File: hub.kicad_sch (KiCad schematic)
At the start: 13 parts, among them J1 USB_C_Receptacle_USB2.0_16P, U1 ADuM4165, U2 USBLC6-2SC6, Y1 24MHz

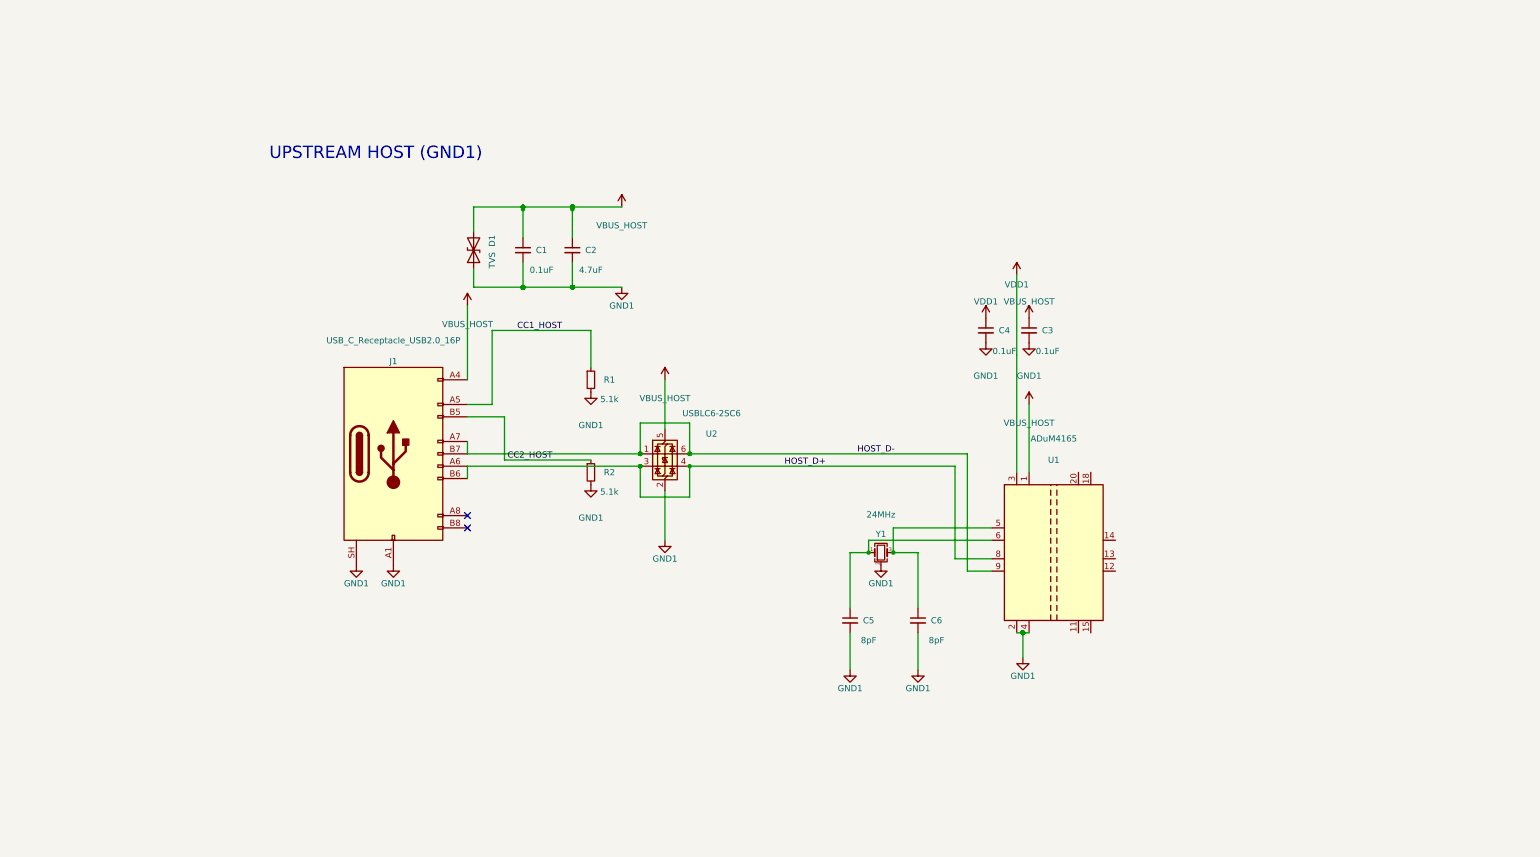
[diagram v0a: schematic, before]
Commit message: feat(revb/sch): upstream CC current-advertisement sensing
Task 4: adds the CC1/CC2 comparator sensing circuit (U3 TLV7042DDFR, R3-R9,
C7-C8, Q1-Q2, D2) that produces HOST_PWR_OK from a VBUS_HOST-referenced
0.66V divider, per decision record section 4.2. Wire-OR polarity is
inverting-comparator + pull-up + NMOS inverter, not the brief's original
either/or. Adds design-note text recording the threshold rationale, the
VBUS_HOST-only constraint, the VCONN false-high caveat, and the R_EN
sizing math.
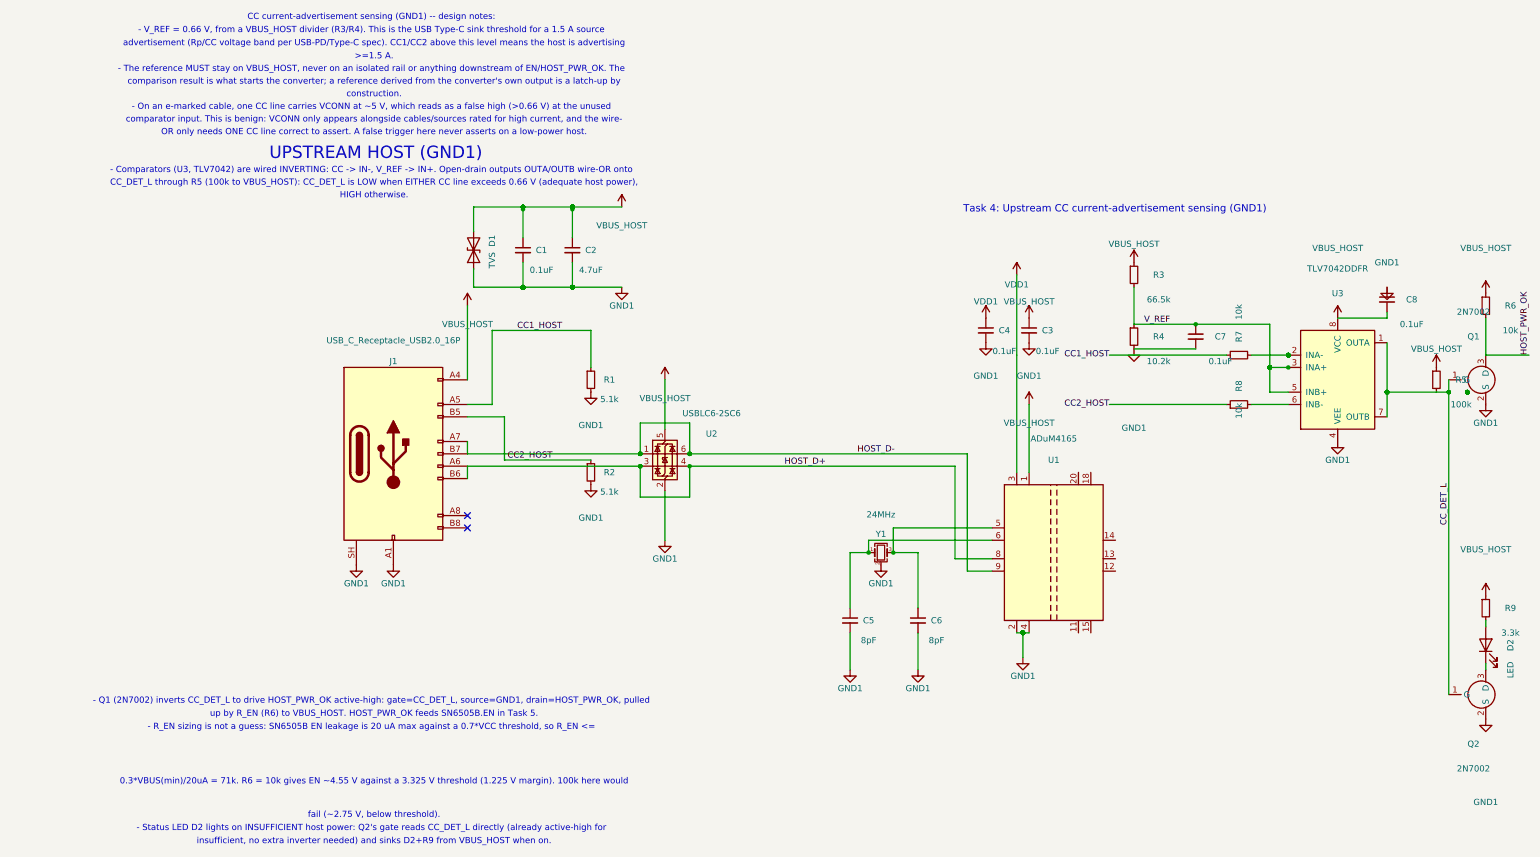
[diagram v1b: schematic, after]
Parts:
- added C7, C8: 0.1uF, symbol Device:C_Small
- added D2: LED, symbol Device:LED
- added Q1, Q2: 2N7002, symbol isolator-lib:2N7002
- added R3: 66.5k, symbol Device:R_Small
- added R4: 10.2k, symbol Device:R_Small
- added R5: 100k, symbol Device:R_Small
- added R6, R7, R8: 10k, symbol Device:R_Small
- added R9: 3.3k, symbol Device:R_Small
- added U3: TLV7042DDFR, symbol isolator-lib:TLV7042DDFR
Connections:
- net CC1_HOST: now also R7.1
- net CC2_HOST: now also R8.1
- net GND1: now also C7.2, C8.1, Q1.2 (S), Q2.2 (S), R4.2, U3.4 (VEE)
- net VBUS_HOST: now also C8.2, R3.1, R5.1, R6.1, R9.1, U3.8 (VCC)
- new net: R8.2, U3.6 (INB-)
- new net: D2.2 (A), R9.2
- new net: D2.1 (K), Q2.3 (D)
- new net: R7.2, U3.2 (INA-)
- new net CC_DET_L: Q1.1 (G), Q2.1 (G), R5.2, U3.1 (OUTA), U3.7 (OUTB)
- new net HOST_PWR_OK: Q1.3 (D), R6.2
- new net V_REF: C7.1, R3.2, R4.1, U3.3 (INA+), U3.5 (INB+)
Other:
- note added: "- Comparators (U3, TLV7042) are wired INVERTING: CC -> IN-, V_REF -> IN+. Open-drain outputs OUTA/OUTB wire-OR onto"
- note added: "- On an e-marked cable, one CC line carries VCONN at ~5 V, which reads as a false high (>0.66 V) at the unused"
- note added: "- Q1 (2N7002) inverts CC_DET_L to drive HOST_PWR_OK active-high: gate=CC_DET_L, source=GND1, drain=HOST_PWR_OK, pulled"
- note added: "- R_EN sizing is not a guess: SN6505B EN leakage is 20 uA max against a 0.7*VCC threshold, so R_EN <="
- note added: "- Status LED D2 lights on INSUFFICIENT host power: Q2's gate reads CC_DET_L directly (already active-high for"
- note added: "- The reference MUST stay on VBUS_HOST, never on an isolated rail or anything downstream of EN/HOST_PWR_OK. The"
- note added: "- V_REF = 0.66 V, from a VBUS_HOST divider (R3/R4). This is the USB Type-C sink threshold for a 1.5 A source"
- note added: "0.3*VBUS(min)/20uA = 71k. R6 = 10k gives EN ~4.55 V against a 3.325 V threshold (1.225 V margin). 100k here would"
- note added: ">=1.5 A."
- note added: "CC current-advertisement sensing (GND1) -- design notes:"
- note added: "CC_DET_L through R5 (100k to VBUS_HOST): CC_DET_L is LOW when EITHER CC line exceeds 0.66 V (adequate host power),"
- note added: "HIGH otherwise."
- note added: "OR only needs ONE CC line correct to assert. A false trigger here never asserts on a low-power host."
- note added: "Task 4: Upstream CC current-advertisement sensing (GND1)"
- note added: "advertisement (Rp/CC voltage band per USB-PD/Type-C spec). CC1/CC2 above this level means the host is advertising"
- note added: "comparator input. This is benign: VCONN only appears alongside cables/sources rated for high current, and the wire-"
- note added: "comparison result is what starts the converter; a reference derived from the converter's own output is a latch-up by"
- note added: "construction."
- note added: "fail (~2.75 V, below threshold)."
- note added: "insufficient, no extra inverter needed) and sinks D2+R9 from VBUS_HOST when on."
- note added: "up by R_EN (R6) to VBUS_HOST. HOST_PWR_OK feeds SN6505B.EN in Task 5."
